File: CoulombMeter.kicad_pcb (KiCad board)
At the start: 2 copper layers, 68 x 60 mm, 19 parts, among them IC1 ATMEGA328P-P, P1 CONN_02X03, P10 CONN_01X03, P2 CONN_01X10, P3 CONN_01X06, P4 USB_OTG, P5 OUTPUT, P6 INPUT, P7 CONN_01X10, P8 OUTPUT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

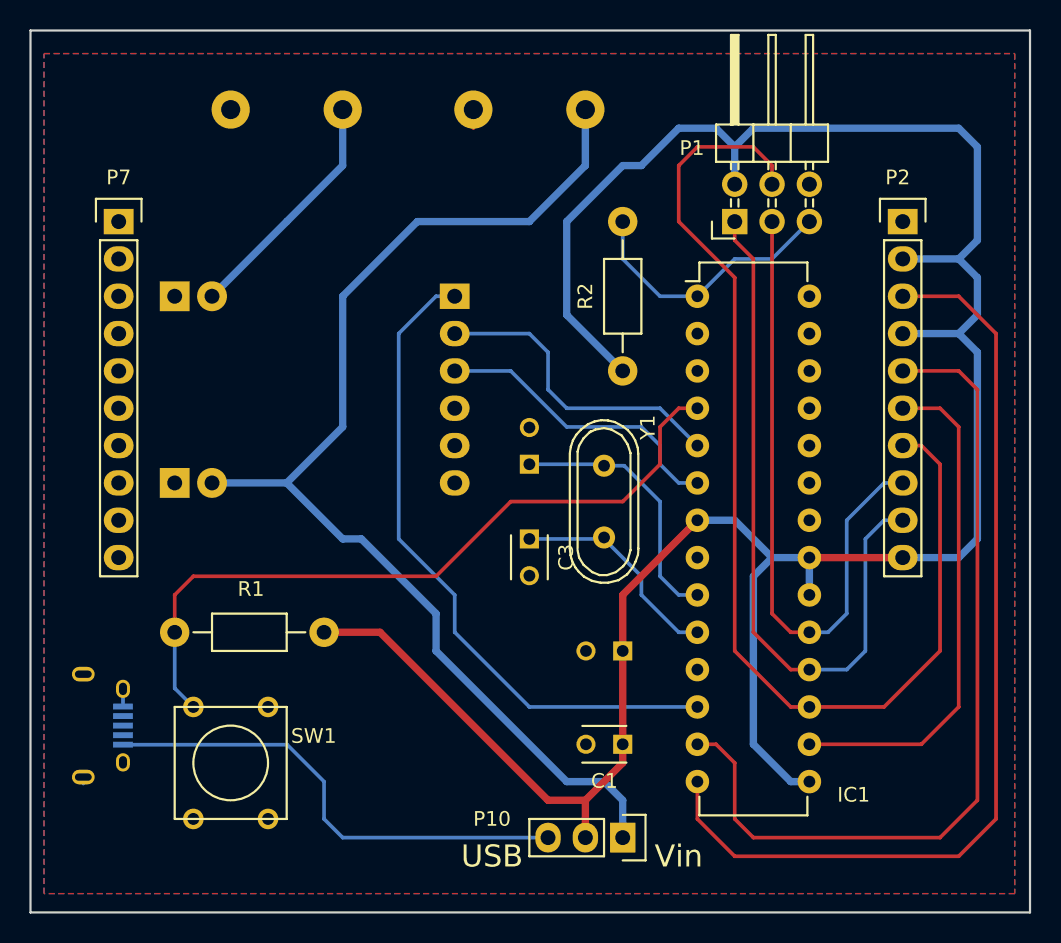
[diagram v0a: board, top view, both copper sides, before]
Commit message: Fix display socket orientation
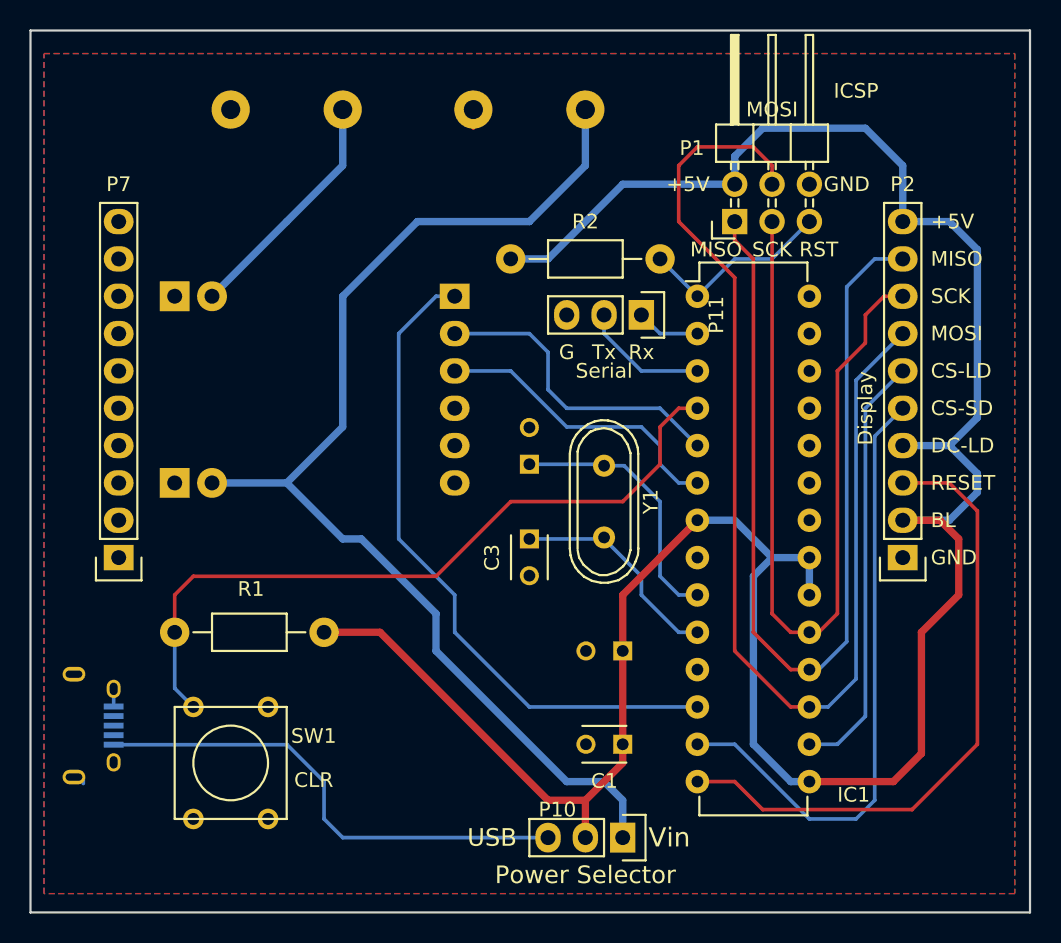
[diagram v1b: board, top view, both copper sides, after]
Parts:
- added P11: Serial, Pin_Headers:Pin_Header_Straight_1x03, F.Cu at (179.1, 96.5)
- C1: value C -> 10n
- C2: value CP -> 10u
- C3, C4: value C -> 15n
- P1: value CONN_02X03 -> ICSP
- P10: value CONN_01X03 -> Supply Sel
- P2: value CONN_01X10 -> Display
- P4: value USB_OTG -> USB +5V
- R1, R2: value R -> 10k
- Y1: value Crystal -> 8MHz
- moved P2 22.9 mm to (196.8, 113.0), turned to 90 degrees
- moved P7 22.9 mm to (143.5, 113.0), turned to 90 degrees
- moved R2 10.8 mm to (170.2, 92.7), turned to 0 degrees
- moved P4 0.64 mm to (141.6, 124.5)
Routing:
- net +5V: track 220.2 -> 196.7 mm
- net /RESET: track 65.4 -> 43.4 mm
- net MISO: track 48.4 -> 65.4 mm
- net /CS-SD: track 58.5 -> 42.2 mm
- net SCK: track 44.0 -> 56.3 mm
- net TXD: track 0.00 -> 8.67 mm
- net /CS-LD: track 34.6 -> 29.1 mm
- net RST: track 18.4 -> 13.3 mm
- net RXD: track 0.00 -> 4.34 mm
- net MOSI: track 76.2 -> 78.7 mm
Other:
- board text added: "+5V"
- board text added: "BL"
- board text added: "CS-LD"
- board text added: "CS-SD"
- board text added: "DC-LD"
- board text added: "G"
- board text added: "GND"
- board text added: "LTC4150"
- board text added: "MISO"
- board text added: "MOSI"
- board text added: "Power Selector"
- board text added: "RESET"
- board text added: "RST"
- board text added: "Rx"
- board text added: "SCK"
- board text added: "Tx"

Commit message: Relocate display
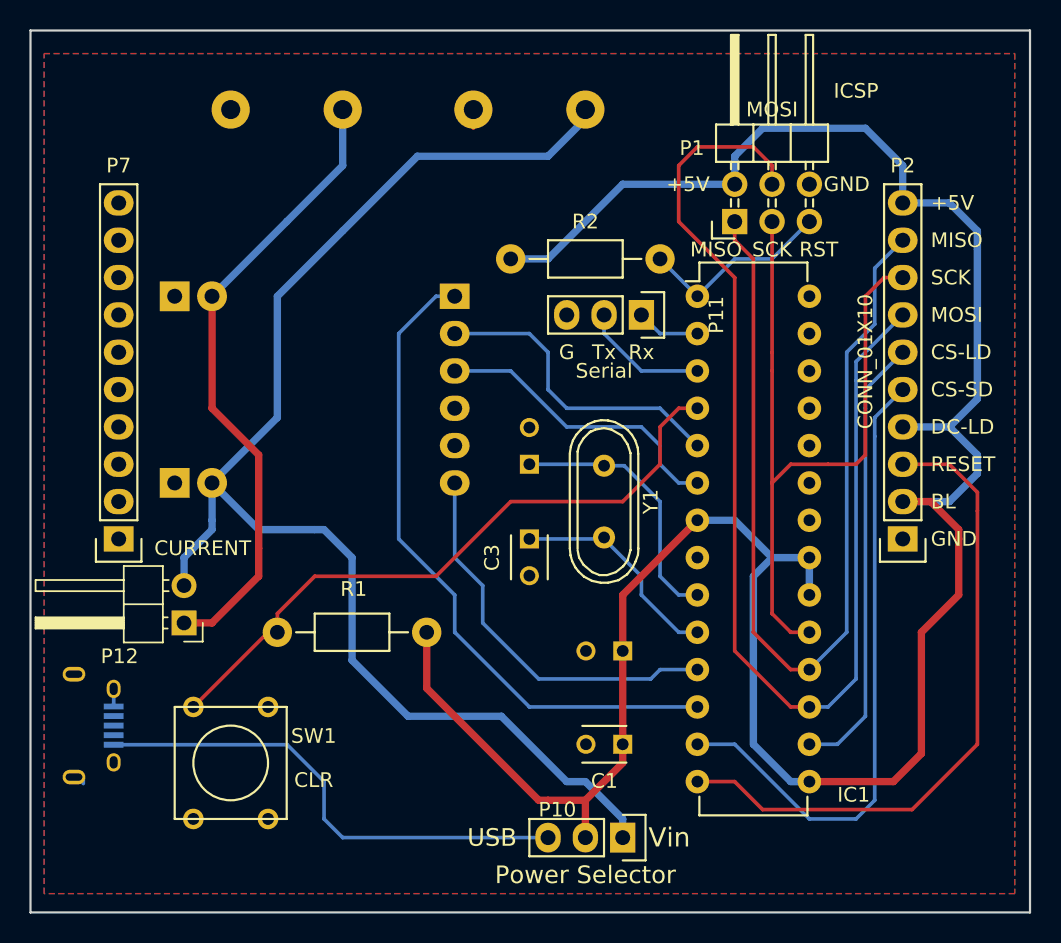
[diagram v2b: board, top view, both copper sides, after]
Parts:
- added P12: CURRENT, Pin_Headers:Pin_Header_Angled_1x02_Pitch2.54mm, F.Cu at (148.0, 117.5)
- P2: value Display -> CONN_01X10
- P4: value USB +5V -> USB_OTG
- moved R1 6.99 mm to (154.3, 118.1)
- moved P2 1.27 mm to (196.8, 111.8)
- moved P7 1.27 mm to (143.5, 111.8)
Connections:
- IC1 pad 11: Net-(IC1-Pad11) -> /SHDN
- P3 pad 6: Net-(P3-Pad6) -> /SHDN
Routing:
- net /SHDN: track 0.00 -> 26.8 mm
- net /POWER_OUT: track 16.4 -> 43.1 mm
- net /POWER_IN: track 79.2 -> 91.7 mm
- net Net-(IC1-Pad4): track 50.5 -> 44.9 mm
- net +5V: track 196.7 -> 191.6 mm
- net SCK: track 56.3 -> 51.4 mm
- net MOSI: track 78.7 -> 80.0 mm
- net /RESET: track 43.4 -> 44.7 mm
- net /CS-SD: track 42.2 -> 43.4 mm
- net /CS-LD: track 29.1 -> 30.4 mm
- net Net-(IC1-Pad25): track 0.00 -> 0.63 mm
